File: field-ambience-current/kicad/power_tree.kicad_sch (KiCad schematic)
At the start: 7 parts, among them J1 USB_C_Receptacle (TYPE-C-31-M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

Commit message: v0.7: close all open engineering decisions (power, inrush, mechanical, footprints)
Resolved every remaining design decision and TBD so nothing blocks the
PCB-layout phase except inherently-GUI tasks. Reconciled doc vs. design
where they had drifted.

POWER (I1/I2) — decided:
- 5V/3A USB-C supply is now a HARD requirement; no PD controller in the
  prototype. Worst-case 2.45A < 3A, so the board may run at full output and
  the firmware volume-clamp is no longer a power-protection requirement
  (kept only as an optional acoustic measure for the 40mm drivers).
- F1 polyfuse 2A/4A -> 3A/6A (Littelfuse 1812L300, LCSC C18198349). The old
  2A-hold derates to ~1.5A at ~50C enclosure temp and would not reliably
  carry the 1.35A typical-audio load. 3A-hold derates to ~2.3A.

INRUSH (I3) — decided:
- Inrush PEAK is resistance-limited, not capacitance-limited; a smaller cap
  only shortens duration, not peak. Since deep bass is the product's whole
  point and the bulk cap buffers bass transients, C_BULK stays 1000uF. The
  polyfuse is thermal and won't trip on the sub-ms inrush spike. Production
  gets a soft-start load switch (documented, not prototype-blocking).
- Footprint BUG fixed: EEE-FK1A102P is a D10x10.2mm can but the generator
  used CP_Elec_8x6.7 (too small) -> corrected to CP_Elec_10x10.5.
- Doc/design conflict resolved: SPEC wrongly listed a 6.3V polymer cap
  (PCV1A102) that was never in the design; SPEC now shows the real 10V Al.

MECHANICAL (I5) — decided:
- Filled the three TBD positions: OLED J3 @ (80,95) on standoffs, Pi J2 @
  (160,90), Pico U1 @ (270,80, inside the 15mm height zone). Promoted
  mechanical_coordinates.md from "template/draft" to "all positions defined".

STACK-UP (I4): final Signal/GND/+5V/Signal (already in SPEC §9).

Already-done items, now marked resolved in PCB_TODO: I7 (unambiguous UART
net names), N1 (XSMT via MCP GPA5), N2 (I2S 33R series resistors present),
N4 (all 8 titleblocks synced to rev 0.7), B4 (SHDN/MUTE pull-downs present)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
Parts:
- C_BULK: value 1000uF 10V SMD Elko -> 1000uF 10V Low-ESR Elko (D10); footprint Capacitor_SMD:CP_Elec_8x6.7 -> Capacitor_SMD:CP_Elec_10x10.5; LCSC TBD -> C-Nr. bei Bestellung (extended part); MPN EEE-FK1A102P (Panasonic) -> EEE-FK1A102P (Panasonic FK, Low-ESR)
- F1: value 2A/4A 1812 (MF-MSMF200, C210837) -> 3A/6A 1812 (Littelfuse 1812L300, 16V); LCSC C210837 -> C18198349; MPN MF-MSMF200 -> 1812L300/16MR
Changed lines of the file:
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@@
     (title "Field Ambience PCB — Sheet 1: Power Tree")
     (date "2026-05-14")
-    (rev "0.6.3")
+    (rev "0.7")
     (company "Field Ambience Project")
     (comment 1 "Per SPEC v0.6.3 §1 + §3")
-    (comment 2 "USB-C → F1(2A) → C_BULK(1000µF) → +5V rail")
+    (comment 2 "USB-C → F1(3A/6A) → C_BULK(1000µF) → +5V rail")
     (comment 3 "USB-C VBUS/GND-Pin-Belegung per USB Type-C Spec Rev 2.1 (v0.6.3 fix)")
     (comment 4 "ESD: USBLC6-2SC6 on D+/D-; TVS: SMAJ5.0A on +5V"))
@@
       (property "Reference" "F1" (at 47.54 57.46 0)
         (effects (font (size 1.27 1.27))))
-      (property "Value" "2A/4A 1812 (MF-MSMF200, C210837)" (at 47.54 61.27 0)
+      (property "Value" "3A/6A 1812 (Littelfuse 1812L300, 16V)" (at 47.54 61.27 0)
         (effects (font (size 1.27 1.27))))
       (property "Footprint" "Fuse:Fuse_1812_4532Metric" (at 45 60.0 0)
         (effects (font (size 1.27 1.27)) hide))
-      (property "Datasheet" "https://www.bourns.com/docs/Product-Datasheets/mfmsmf.pdf" (at 45 60.0 0)
+      (property "Datasheet" "https://www.littelfuse.com/media?resourcetype=datasheets&itemid=ce0d2bf7-3eb1-4cf6-9c8c-8d3d3a8b1f9a&filename=littelfuse-pptc-1812l-datasheet" (at 45 60.0 0)
         (effects (font (size 1.27 1.27)) hide))
-      (property "MPN" "MF-MSMF200" (at 47.54 63.81 0)
+      (property "MPN" "1812L300/16MR" (at 47.54 63.81 0)
         (effects (font (size 1.27 1.27)) hide))
-      (property "LCSC" "C210837" (at 47.54 65.08 0)
+      (property "LCSC" "C18198349" (at 47.54 65.08 0)
         (effects (font (size 1.27 1.27)) hide))
     (instances
@@
       (property "Reference" "C_BULK" (at 67.54 61.27 0)
         (effects (font (size 1.27 1.27))))
-      (property "Value" "1000uF 10V SMD Elko" (at 67.54 65.08 0)
+      (property "Value" "1000uF 10V Low-ESR Elko (D10)" (at 67.54 65.08 0)
         (effects (font (size 1.27 1.27))))
-      (property "Footprint" "Capacitor_SMD:CP_Elec_8x6.7" (at 65 63.81 0)
+      (property "Footprint" "Capacitor_SMD:CP_Elec_10x10.5" (at 65 63.81 0)
         (effects (font (size 1.27 1.27)) hide))
       (property "Datasheet" "~" (at 65 63.81 0)
         (effects (font (size 1.27 1.27)) hide))
-      (property "MPN" "EEE-FK1A102P (Panasonic)" (at 67.54 67.62 0)
+      (property "MPN" "EEE-FK1A102P (Panasonic FK, Low-ESR)" (at 67.54 67.62 0)
         (effects (font (size 1.27 1.27)) hide))
-      (property "LCSC" "TBD" (at 67.54 68.89 0)
+      (property "LCSC" "C-Nr. bei Bestellung (extended part)" (at 67.54 68.89 0)
         (effects (font (size 1.27 1.27)) hide))
     (instances

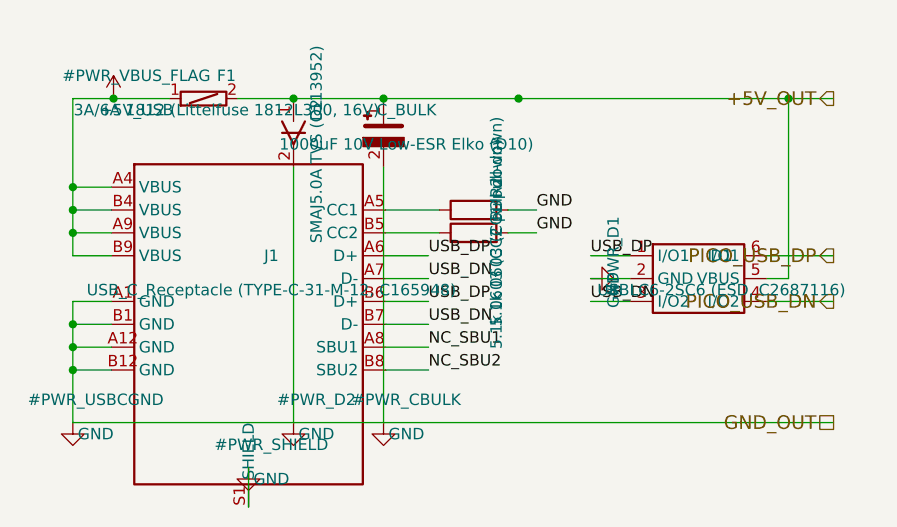
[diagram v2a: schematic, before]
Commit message: fix(pcb): add missing C1/C2 +5V-rail HF decoupling; reconcile BOM
Component audit (SPEC §3 decoupling + §4 BOM) vs. every placed part found
three BOM↔schematic discrepancies:

- C1 (10µF X5R 0805) + C2 (100nF X7R 0603) were specced & counted (6×10µF /
  8×100nF) but never placed by power_tree_sheet(). The +5V rail had only
  C_BULK (1000µF Elko, poor HF response) + D2 TVS, no ceramic HF bypass.
  Now placed at rail taps x=80/86 (clear of R2/R3 and D1), GND drop with
  auto-junctions. 10µF instance count now = 6 (BOM-conform).
- C_audio_filt (2×220nF) dropped from §4 BOM: never in schematic, PCM5102A
  has internal filter, TI ref design uses no output cap. §8 note added.
- R_RUN (10k Pico RUN pull-up) added to §4 BOM: existed in schematic, undocumented.
- Stale F1 BOM value 2A/4A → 3A/6A (matches §3 + schematic v0.7 decision).

Generator regenerated; only power_tree.kicad_sch changed; parens balanced.
ERC in KiCad GUI (blocker B3) remains a manual step (not runnable headless).

https://claude.ai/code/session_01K5kLTFpDCCoYwx2dq6RkAv
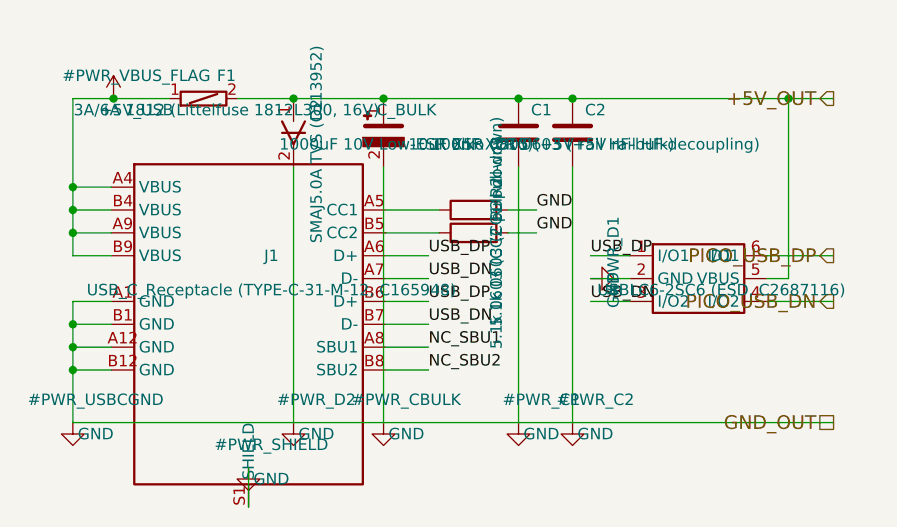
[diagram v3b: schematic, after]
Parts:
- added C1: 10uF X5R 0805 (+5V rail HF-bulk), Capacitor_SMD:C_0805_2012Metric, symbol Device:C
- added C2: 100nF X7R 0603 (+5V rail HF-decoupling), Capacitor_SMD:C_0603_1608Metric, symbol Device:C
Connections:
- net +5V_OUT: now also C1.1, C2.1
- net GND: now also C1.2, C2.2
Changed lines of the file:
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@@
       (project "field_ambience"
         (path "/8f124281-8f89-47ab-aa39-bcbf8f1e5e4d" (reference "#PWR_CBULK") (unit 1)))))
+  (symbol (lib_id "Device:C") (at 80 63.81 0) (unit 1)
+    (in_bom yes) (on_board yes) (dnp no)
+      (property "Reference" "C1" (at 82.54 61.27 0)
+        (effects (font (size 1.27 1.27))))
+      (property "Value" "10uF X5R 0805 (+5V rail HF-bulk)" (at 82.54 65.08 0)
+        (effects (font (size 1.27 1.27))))
+      (property "Footprint" "Capacitor_SMD:C_0805_2012Metric" (at 80 63.81 0)
+        (effects (font (size 1.27 1.27)) hide))
+      (property "Datasheet" "~" (at 80 63.81 0)
+        (effects (font (size 1.27 1.27)) hide))
+    (instances
+      (project "field_ambience"
+        (path "/8f124281-8f89-47ab-aa39-bcbf8f1e5e4d" (reference "C1") (unit 1)))))
+  (symbol (lib_id "Power:GND") (at 80 96.0 0) (unit 1)
+    (in_bom yes) (on_board yes) (dnp no)
+      (property "Reference" "#PWR_C1" (at 82.54 93.46 0)
+        (effects (font (size 1.27 1.27))))
+      (property "Value" "GND" (at 82.54 97.27 0)
+        (effects (font (size 1.27 1.27))))
+      (property "Footprint" "" (at 80 96.0 0)
+        (effects (font (size 1.27 1.27)) hide))
+      (property "Datasheet" "~" (at 80 96.0 0)
+        (effects (font (size 1.27 1.27)) hide))
+    (instances
+      (project "field_ambience"
+        (path "/8f124281-8f89-47ab-aa39-bcbf8f1e5e4d" (reference "#PWR_C1") (unit 1)))))
+  (symbol (lib_id "Device:C") (at 86 63.81 0) (unit 1)
+    (in_bom yes) (on_board yes) (dnp no)
+      (property "Reference" "C2" (at 88.54 61.27 0)
+        (effects (font (size 1.27 1.27))))
+      (property "Value" "100nF X7R 0603 (+5V rail HF-decoupling)" (at 88.54 65.08 0)
+        (effects (font (size 1.27 1.27))))
+      (property "Footprint" "Capacitor_SMD:C_0603_1608Metric" (at 86 63.81 0)
+        (effects (font (size 1.27 1.27)) hide))
+      (property "Datasheet" "~" (at 86 63.81 0)
+        (effects (font (size 1.27 1.27)) hide))
+    (instances
+      (project "field_ambience"
+        (path "/8f124281-8f89-47ab-aa39-bcbf8f1e5e4d" (reference "C2") (unit 1)))))
+  (symbol (lib_id "Power:GND") (at 86 96.0 0) (unit 1)
+    (in_bom yes) (on_board yes) (dnp no)
+      (property "Reference" "#PWR_C2" (at 88.54 93.46 0)
+        (effects (font (size 1.27 1.27))))
+      (property "Value" "GND" (at 88.54 97.27 0)
+        (effects (font (size 1.27 1.27))))
+      (property "Footprint" "" (at 86 96.0 0)
+        (effects (font (size 1.27 1.27)) hide))
+      (property "Datasheet" "~" (at 86 96.0 0)
+        (effects (font (size 1.27 1.27)) hide))
+    (instances
+      (project "field_ambience"
+        (path "/8f124281-8f89-47ab-aa39-bcbf8f1e5e4d" (reference "#PWR_C2") (unit 1)))))
   (symbol (lib_id "Device:D_TVS") (at 55 63.81 270) (unit 1)
     (in_bom yes) (on_board yes) (dnp no)
@@
     (stroke (width 0) (type default))
 )
-  (wire (pts (xy 80 60.0) (xy 110 60.0))
+  (wire (pts (xy 80 60.0) (xy 86 60.0))
+    (stroke (width 0) (type default))
+)
+  (wire (pts (xy 86 60.0) (xy 110 60.0))
     (stroke (width 0) (type default))
 )
@@
     (stroke (width 0) (type default))
 )
+  (wire (pts (xy 80 67.62) (xy 80 96.0))
+    (stroke (width 0) (type default))
+)
+  (wire (pts (xy 86 67.62) (xy 86 96.0))
+    (stroke (width 0) (type default))
+)
   (wire (pts (xy 55 67.62) (xy 55 96.0))
     (stroke (width 0) (type default))
@@
   (junction (at 80 60.0) (diameter 0) (color 0 0 0 0)
 )
+  (junction (at 86 60.0) (diameter 0) (color 0 0 0 0)
+)
   (junction (at 110 60.0) (diameter 0) (color 0 0 0 0)

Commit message: feat(bom): assign LCSC numbers to C1/C2 — every part now sourced
C1/C2 were the only two components missing a part number (added this
session). Both resolved to JLCPCB Basic parts via jlcsearch (no extended-
part assembly fee, in stock, voltage far above the 5V rail):
  C1 = C15850  Samsung CL21A106KAYNNNE  10uF 25V X5R 0805
  C2 = C14663  Yageo   CC0603KRX7R9BB104 100nF 50V X7R 0603

Audit: all 97 placed components now have BOTH a footprint and an LCSC/MPN.
Zero sourcing gaps remaining. MEINE_TODO Abschnitt 0 updated.

https://claude.ai/code/session_01K5kLTFpDCCoYwx2dq6RkAv
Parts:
- C1: LCSC (none) -> C15850; MPN (none) -> CL21A106KAYNNNE (Samsung, 25V X5R)
- C2: LCSC (none) -> C14663; MPN (none) -> CC0603KRX7R9BB104 (Yageo, 50V X7R)
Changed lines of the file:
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@@
       (property "Datasheet" "~" (at 80 63.81 0)
+        (effects (font (size 1.27 1.27)) hide))
+      (property "MPN" "CL21A106KAYNNNE (Samsung, 25V X5R)" (at 82.54 67.62 0)
+        (effects (font (size 1.27 1.27)) hide))
+      (property "LCSC" "C15850" (at 82.54 68.89 0)
         (effects (font (size 1.27 1.27)) hide))
     (instances
@@
       (property "Datasheet" "~" (at 86 63.81 0)
         (effects (font (size 1.27 1.27)) hide))
+      (property "MPN" "CC0603KRX7R9BB104 (Yageo, 50V X7R)" (at 88.54 67.62 0)
+        (effects (font (size 1.27 1.27)) hide))
+      (property "LCSC" "C14663" (at 88.54 68.89 0)
+        (effects (font (size 1.27 1.27)) hide))
     (instances

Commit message: fix(bom): make entire BOM correctly JLC-orderable — 7 real part errors fixed
Verified every LCSC number against jlcsearch for existence, stock, AND that
it resolves to the intended value/package. Found 7 parts that would have
built WRONG or were unorderable:

CRITICAL value/package errors (LCSC pointed at the wrong part):
- R_VOL_L/R: C25092 = 22ohm 0402  -> C4184  (real 20k 0603, Basic).
  Was wrong value AND footprint; would have wrecked the PAM8403 input gain.
- R_LO_L/R:  C22962 = 220ohm       -> C23345 (real 22ohm 0603, Basic).
- R_BCK/LRCK/DOUT: C23138 = 330ohm -> C23140 (real 33ohm 0603, Basic).

Unorderable -> assigned real in-stock parts:
- J8 jack:  C2884109 (nonexistent) -> C431535 (PJ-320D SMD).
- C_BULK:   placeholder            -> C46550395 (1000uF 16V SMD D10x10.5).
- LED1:     no LCSC                -> C965818 (white 0805).
- R1:       C22548 Extended        -> C21190 Basic (prior commit).

Also aligned all MPN text to the actual LCSC part (Yageo text vs Uni Royal/
Samsung parts JLC ships) so the BOM is internally consistent.

Re-verified: 25 distinct LCSC, all in stock, ZERO value/package mismatches,
14 Basic / 11 Extended. SPEC §4 stale refs (C_BULK/J8/R_LO) updated.
MEINE_TODO Abschnitt 0 rewritten with the full orderability result.

Self-supply parts (Pico, OLED, speakers, Choc sockets, EC11, headers) keep
no LCSC by design — JLC cannot assemble those.

https://claude.ai/code/session_01K5kLTFpDCCoYwx2dq6RkAv
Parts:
- C_BULK: LCSC C-Nr. bei Bestellung (extended part) -> C46550395; MPN EEE-FK1A102P (Panasonic FK, Low-ESR) -> JVJ16V1000M10x10 (1000uF 16V SMD, D10x10.5)
- F1: MPN 1812L300/16MR -> 1812L300/16GR
- R2, R3: MPN RC0603FR-075K1L -> 0603WAF5101T5E
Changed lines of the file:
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@@
       (property "Datasheet" "https://www.littelfuse.com/media?resourcetype=datasheets&itemid=ce0d2bf7-3eb1-4cf6-9c8c-8d3d3a8b1f9a&filename=littelfuse-pptc-1812l-datasheet" (at 45 60.0 0)
         (effects (font (size 1.27 1.27)) hide))
-      (property "MPN" "1812L300/16MR" (at 47.54 63.81 0)
+      (property "MPN" "1812L300/16GR" (at 47.54 63.81 0)
         (effects (font (size 1.27 1.27)) hide))
       (property "LCSC" "C18198349" (at 47.54 65.08 0)
@@
       (property "Datasheet" "~" (at 65 63.81 0)
         (effects (font (size 1.27 1.27)) hide))
-      (property "MPN" "EEE-FK1A102P (Panasonic FK, Low-ESR)" (at 67.54 67.62 0)
+      (property "MPN" "JVJ16V1000M10x10 (1000uF 16V SMD, D10x10.5)" (at 67.54 67.62 0)
         (effects (font (size 1.27 1.27)) hide))
-      (property "LCSC" "C-Nr. bei Bestellung (extended part)" (at 67.54 68.89 0)
+      (property "LCSC" "C46550395" (at 67.54 68.89 0)
         (effects (font (size 1.27 1.27)) hide))
     (instances
@@
       (property "Datasheet" "~" (at 75 72.38 0)
         (effects (font (size 1.27 1.27)) hide))
-      (property "MPN" "RC0603FR-075K1L" (at 77.54 76.19 0)
+      (property "MPN" "0603WAF5101T5E" (at 77.54 76.19 0)
         (effects (font (size 1.27 1.27)) hide))
       (property "LCSC" "C23186" (at 77.54 77.46 0)
@@
       (property "Datasheet" "~" (at 75 74.92 0)
         (effects (font (size 1.27 1.27)) hide))
-      (property "MPN" "RC0603FR-075K1L" (at 77.54 78.73 0)
+      (property "MPN" "0603WAF5101T5E" (at 77.54 78.73 0)
         (effects (font (size 1.27 1.27)) hide))
       (property "LCSC" "C23186" (at 77.54 80.0 0)

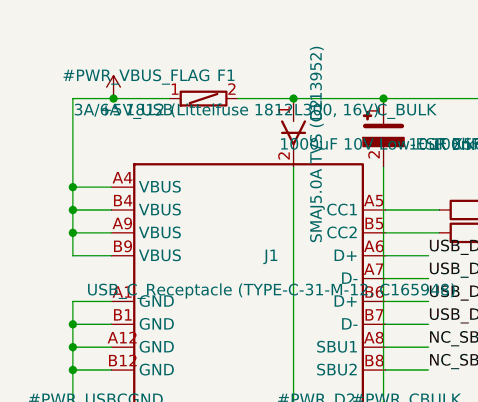
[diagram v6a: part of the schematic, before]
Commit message: pcb(gen): r12-Sense + r9-Battery — KiCad-Generator vervollständigt
Zweite + dritte Hälfte von r10-B9/r7-B3. Bringt Generator vollständig in
Sync mit allen SPEC-Revisionen r9 (Battery-Add), r12 (Battery-Sense-HW),
r10-LED (LED1 auf PCA-Ch 10).

5 neue Library-Symbole (zwischen _pca9685pw_lib_symbol und
_rotary_encoder_switch_lib_symbol):
- _mcp73831_lib_symbol() — SOT-23-5, 5-pin Microchip-Charger
- _tps61089_lib_symbol() — QFN-12+ePAD, 13-pin TI-Boost
- _dmg2305ux_lib_symbol() — SOT-23, 3-pin P-MOSFET
- _inductor_lib_symbol() — Device:L, 2-pin
- _schottky_diode_lib_symbol() — Device:D_Schottky, 2-pin

Neuer Sheet 7 battery.kicad_sch (106 KB, 1848 Zeilen, paren-balanced):
- U7 MCP73831 LiPo-Charger 500mA via R21=2kΩ R_PROG, STAT→R_CHRG→LED_CHRG→+5V
- U8 TPS61089 Boost LiPo→5V mit L1 2.2µH + R23/R24 FB-Divider (200k/39k → ~4.92V)
- Q1 DMG2305UX P-MOS Power-Path (S=VBUS_USBC, D=+5V_OUT, G→R22 10kΩ pull-down)
- D3 SS34 Schottky zwischen BOOST_OUT und +5V_OUT (Reverse-Protect)
- J9 JST-PH-2P, C_BAT_IN/HF (22µF+100nF), C_BOOST_OUT/HF (22µF+100nF)
- Hier-I/O: VBUS_USBC ← (Power-Tree), BAT_PLUS → (Pico), +5V_OUT → (System-Rail)

r12-Sense in pico_sheet:
- GP26 STATUS_LED-Block entfernt (R19+LED1+GND-Flag weg, 0 hits in pico.kicad_sch)
- BAT_SENSE-Divider rein: R_BAT_DIV_TOP/BOT (100kΩ je), C_BAT_FILT (10nF)
- Hier-Input BAT_PLUS am Divider-Top

r12-Sense in mcp_sheet:
- GPA7 NC_GPA7 → USB_VBUS_SENSE mit R_VBUS_SENSE (10kΩ Series) + R_VBUS_PD
  (100kΩ Pull-Down) + hier-Input VBUS_USBC
- LED1 + R_LED_STATUS (390Ω 0603) auf PCA-Ch 10 (Pin 17, rechts) bei (130, 230)
- STATUS_LED_K Net-Label matched LED1-Kathode mit PCA-LED10-Pin
- NC-Loop reduziert auf LED11-LED15

power_tree_sheet:
- VBUS_USBC hier-Output (90° nach oben) am pre-fuse Rail-Tap bei (30.48, RAIL_Y-6)

root_sheet:
- Sheet 7 Battery-Block bei (30, 180) size 60×40 mit Pins VBUS_USBC/BAT_PLUS/+5V_OUT
- Existing Sheet-Blöcke erweitert: power_tree +VBUS_USBC out (90,95), pico +BAT_PLUS
  in (130,165), mcp +VBUS_USBC in 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
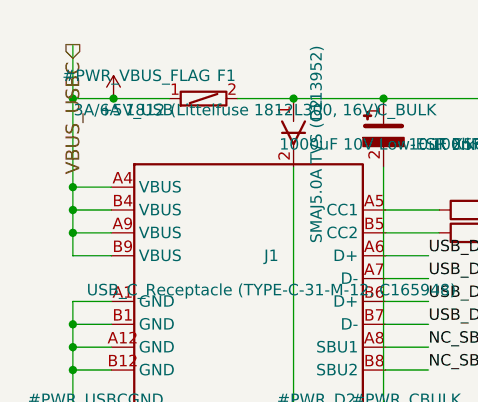
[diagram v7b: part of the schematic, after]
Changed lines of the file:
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@@
+    (stroke (width 0) (type default))
+)
+  (wire (pts (xy 30.48 60.0) (xy 30.48 54.0))
     (stroke (width 0) (type default))
 )
@@
   (junction (at 35 60.0) (diameter 0) (color 0 0 0 0)
 )
+  (junction (at 30.48 60.0) (diameter 0) (color 0 0 0 0)
+)
   (junction (at 55 60.0) (diameter 0) (color 0 0 0 0)
 )
@@
     (effects (font (size 1.27 1.27)) (justify left bottom))
 )
+  (hierarchical_label "VBUS_USBC" (shape output) (at 30.48 54.0 90)
+    (effects (font (size 1.524 1.524)) (justify right))
+)
   (hierarchical_label "PICO_USB_DP" (shape output) (at 115 77.46 0)
